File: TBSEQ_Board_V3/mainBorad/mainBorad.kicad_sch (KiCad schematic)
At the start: 0 parts

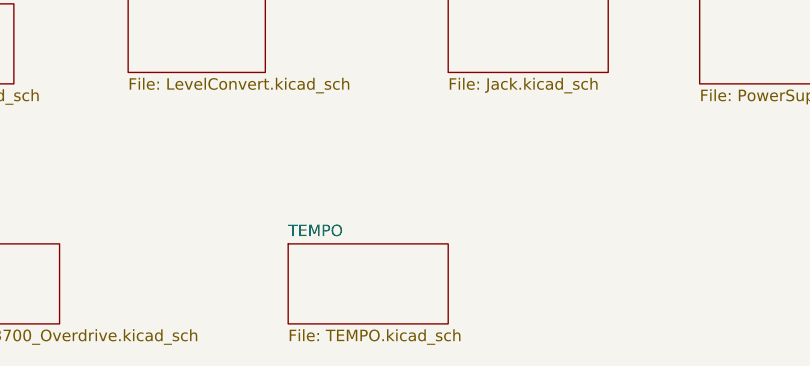
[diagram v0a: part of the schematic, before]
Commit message: V3Board
DualTr フットプリント変更
配線ミス修正
TEMPO削除⇒PanelBoardに移動
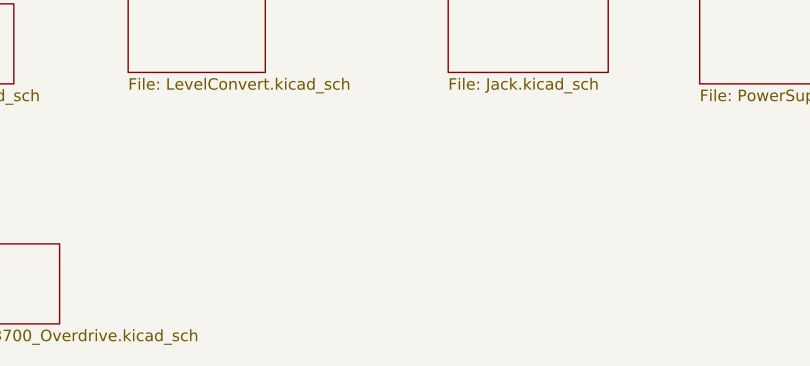
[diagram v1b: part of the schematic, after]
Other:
- removed sheet TEMPO
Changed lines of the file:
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@@
-		)
-	)
-	(sheet
-		(at 158.75 50.8)
-		(size 17.78 8.89)
-		(fields_autoplaced yes)
-		(stroke
-			(width 0.1524)
-			(type solid)
-		)
-		(fill
-			(color 0 0 0 0.0000)
-		)
-		(property "Sheetname" "TEMPO"
-			(at 158.75 50.0884 0)
-			(effects
-				(font
-					(size 1.27 1.27)
-				)
-				(justify left bottom)
-			)
-		)
-		(property "Sheetfile" "TEMPO.kicad_sch"
-			(at 158.75 60.2746 0)
-			(effects
-				(font
-					(size 1.27 1.27)
-				)
-				(justify left top)
-			)
-		)
-		(instances
-			(project "mainBorad"
-				(path "/83af791a-9776-40a7-82ad-9528ff7474b8"
-					(page "13")
-				)
-			)
 		)
 	)

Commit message: V3Board
アートワーク中
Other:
- sheet MIDIRx renamed MIDIRxTx
- added sheet TEMPO (TEMPO.kicad_sch)
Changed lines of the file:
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@@
+	)
+	(sheet
+		(at 160.02 49.53)
+		(size 15.24 8.89)
+		(fields_autoplaced yes)
+		(stroke
+			(width 0.1524)
+			(type solid)
+		)
+		(fill
+			(color 0 0 0 0.0000)
+		)
+		(property "Sheetname" "TEMPO"
+			(at 160.02 48.8184 0)
+			(effects
+				(font
+					(size 1.27 1.27)
+				)
+				(justify left bottom)
+			)
+		)
+		(property "Sheetfile" "TEMPO.kicad_sch"
+			(at 160.02 59.0046 0)
+			(effects
+				(font
+					(size 1.27 1.27)
+				)
+				(justify left top)
+			)
+		)
+		(instances
+			(project "mainBorad"
+				(path "/83af791a-9776-40a7-82ad-9528ff7474b8"
+					(page "13")
+				)
+			)
+		)
 	)
 	(sheet
@@
 			(color 0 0 0 0.0000)
 		)
-		(property "Sheetname" "MIDIRx"
+		(property "Sheetname" "MIDIRxTx"
 			(at 54.61 20.8784 0)
 			(effects
